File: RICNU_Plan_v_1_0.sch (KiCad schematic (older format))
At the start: 0 parts

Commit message: Re-routed CAN, RS-485, and debug connectors (wrong polarity in all)
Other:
- note added: "*"
- note added: "A and B for SN65HVD75 are \nopposite of RS-485 standard"
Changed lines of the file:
@@
 F0 "RS485 Transceiver" 60
 F1 "RICNU_Plan_v_1_0_RS485.sch" 60
-F2 "RS485.A" B L 3800 4500 60
-F3 "RS485.B" B L 3800 4600 60
+F2 "RS485.A" B L 3800 4600 60
+F3 "RS485.B" B L 3800 4500 60
 F4 "RS485.#RE" I R 5500 4700 60
 F5 "RS485.DE" I R 5500 4600 60
@@
 F4 "SWD.RESET" O R 3100 3300 60
 $EndSheet
+Text Notes 2800 6700 0    60   ~ 0
+A and B for SN65HVD75 are \nopposite of RS-485 standard
+Text Notes 4300 4500 0    60   ~ 0
+*
+Text Notes 2700 6600 0    60   ~ 0
+*
 $EndSCHEMATC

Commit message: Added connections to monitor power, changed CANSTB MCU pin, moved LED pins around
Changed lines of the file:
@@
 $EndDescr
 $Sheet
-S 3798 5702 1702 298
+S 3798 5902 1702 298
 U 59D46777
 F0 "Power Conditioning" 60
@@
 $EndSheet
 $Sheet
-S 6200 5150 1700 850
+S 6200 5350 1700 850
 U 59E3791C
 F0 "Bus Driver" 60
 F1 "RICNU_Plan_v_1_0_UARTDriver.sch" 60
-F2 "UMUX.BT.TX" I R 7900 5800 60
-F3 "UMUX.BT.RX" O R 7900 5900 60
-F4 "UMUX.U2U.RX" O L 6200 5250 60
-F5 "UMUX.U2U.TX" I L 6200 5350 60
-F6 "UMUX.MCU.RX" O R 7900 5250 60
-F7 "UMUX.MCU.TX" I R 7900 5350 60
-F8 "UMUX.BT.BOOT" O R 7900 5700 60
-$EndSheet
-$Sheet
-S 3800 5150 1700 300
+F2 "UMUX.BT.TX" I R 7900 6000 60
+F3 "UMUX.BT.RX" O R 7900 6100 60
+F4 "UMUX.U2U.RX" O L 6200 5450 60
+F5 "UMUX.U2U.TX" I L 6200 5550 60
+F6 "UMUX.MCU.RX" O R 7900 5450 60
+F7 "UMUX.MCU.TX" I R 7900 5550 60
+F8 "UMUX.BT.BOOT" O R 7900 5900 60
+$EndSheet
+$Sheet
+S 3800 5150 1700 500
 U 59D3E543
 F0 "USB to UART" 60
 F1 "RICNU_Plan_v_1_0_USB2UART.sch" 60
-F2 "U2U.TX" O R 5500 5350 60
-F3 "U2U.RX" I R 5500 5250 60
+F2 "U2U.TX" O R 5500 5550 60
+F3 "U2U.RX" I R 5500 5450 60
 F4 "U2U.USB.DP" B L 3800 5250 60
 F5 "U2U.USB.DM" B L 3800 5350 60
+F6 "U2U.PWREN" O R 5500 5250 60
+F7 "U2U.USBON" O R 5500 5350 60
 $EndSheet
 $Sheet
@@
 Series protection resistor included in "Breakout"
 $Sheet
-S 8600 5600 1700 400
+S 8600 5800 1700 400
 U 59D3E54A
 F0 "Bluetooth" 60
 F1 "RICNU_Plan_v_1_0_Bluetooth.sch" 60
-F2 "BT.BOOT0" I L 8600 5700 60
-F3 "BT.RX" I L 8600 5900 60
-F4 "BT.TX" O L 8600 5800 60
+F2 "BT.BOOT0" I L 8600 5900 60
+F3 "BT.RX" I L 8600 6100 60
+F4 "BT.TX" O L 8600 6000 60
 $EndSheet
 Text Notes 6750 9100 0    60   ~ 0
@@
 Open copper ring around the periphery of the board\nstitched throughout with vias & connected to USB shield \nand SD card shield. - ESD protection and edge EMC.\nAn external ESD strike will prefer the ring/shield casing for SD/USB instead \nof the components, and will be either earthed if connected to PC+wall\nor discharged into board ground via multiple small caps (see SD and USB).\nIf on the knee, discharged into the screw(s?) and into the metal leg
 $Sheet
-S 6200 1400 1700 3500
+S 6200 1400 1700 3700
 U 59D3E349
 F0 "MCU" 60
@@
 F42 "MCU.PC7" B R 7900 1900 60
 F43 "MCU.PA0" B R 7900 1500 60
+F44 "MCU.PWREN" I L 6200 4900 60
+F45 "MCU.USBON" I L 6200 5000 60
 $EndSheet
 Text Notes 10400 9200 0    60   ~ 0
@@
 	5500 4800 6200 4800
 Wire Wire Line
-	5500 5250 6200 5250
-Wire Wire Line
-	5500 5350 6200 5350
-Wire Wire Line
-	7900 5250 8600 5250
-Wire Wire Line
-	8600 5250 8600 4800
+	5500 5450 6200 5450
+Wire Wire Line
+	5500 5550 6200 5550
+Wire Wire Line
+	7900 5450 8600 5450
+Wire Wire Line
+	8600 5450 8600 4800
 Wire Wire Line
 	8600 4800 7900 4800
@@
 	7900 4700 8700 4700
 Wire Wire Line
-	8700 4700 8700 5350
-Wire Wire Line
-	8700 5350 7900 5350
-Wire Wire Line
-	8600 5700 7900 5700
-Wire Wire Line
-	8600 5800 7900 5800
+	8700 4700 8700 5550
+Wire Wire Line
+	8700 5550 7900 5550
 Wire Wire Line
 	8600 5900 7900 5900
+Wire Wire Line
+	8600 6000 7900 6000
+Wire Wire Line
+	8600 6100 7900 6100
 $Sheet
 S 8600 1400 1700 1700
@@
 Text Label 5550 4800 0    60   ~ 0
 RS485_RX
-Text Label 5550 5250 0    60   ~ 0
+Text Label 5550 5450 0    60   ~ 0
 FTDI_UART_RX
-Text Label 5550 5350 0    60   ~ 0
+Text Label 5550 5550 0    60   ~ 0
 FTDI_UART_TX
 Text Label 3150 5250 0    60   ~ 0
@@
 Text Label 3150 4500 0    60   ~ 0
 RS485_D+
-Text Label 7950 5350 0    60   ~ 0
+Text Label 7950 5550 0    60   ~ 0
 MCU_UART_TX
-Text Label 7950 5250 0    60   ~ 0
+Text Label 7950 5450 0    60   ~ 0
 MCU_UART_RX
-Text Label 7950 5700 0    60   ~ 0
+Text Label 7950 5800 0    60   ~ 0
 BT_BOOT0
-Text Label 7950 5800 0    60   ~ 0
+Text Label 7950 5900 0    60   ~ 0
 BT_UART_TX
-Text Label 7950 5900 0    60   ~ 0
+Text Label 7950 6000 0    60   ~ 0
 BT_UART_RX
 Wire Wire Line
@@
 DIO16
 $Sheet
-S 1400 5700 1700 300
+S 1400 5900 1700 300
 U 59FC1385
 F0 "5V Power Input Connector" 60
@@
 Text Notes 2700 6600 0    60   ~ 0
 *
+Wire Wire Line
+	6200 4900 6000 4900
+Wire Wire Line
+	6000 4900 6000 5250
+Wire Wire Line
+	6000 5250 5500 5250
+Wire Wire Line
+	5500 5350 6100 5350
+Wire Wire Line
+	6100 5350 6100 5000
+Wire Wire Line
+	6100 5000 6200 5000
+Text Label 5550 5350 0    60   ~ 0
+FTDI_USBON
+Text Label 5550 5250 0    60   ~ 0
+FTDI_PWREN
 $EndSCHEMATC

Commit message: Design freeze - ordered the board
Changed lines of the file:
@@
 Text Label 7950 5450 0    60   ~ 0
 MCU_UART_RX
-Text Label 7950 5800 0    60   ~ 0
+Text Label 8000 5900 0    60   ~ 0
 BT_BOOT0
-Text Label 7950 5900 0    60   ~ 0
+Text Label 8000 6000 0    60   ~ 0
 BT_UART_TX
-Text Label 7950 6000 0    60   ~ 0
+Text Label 8000 6100 0    60   ~ 0
 BT_UART_RX
 Wire Wire Line

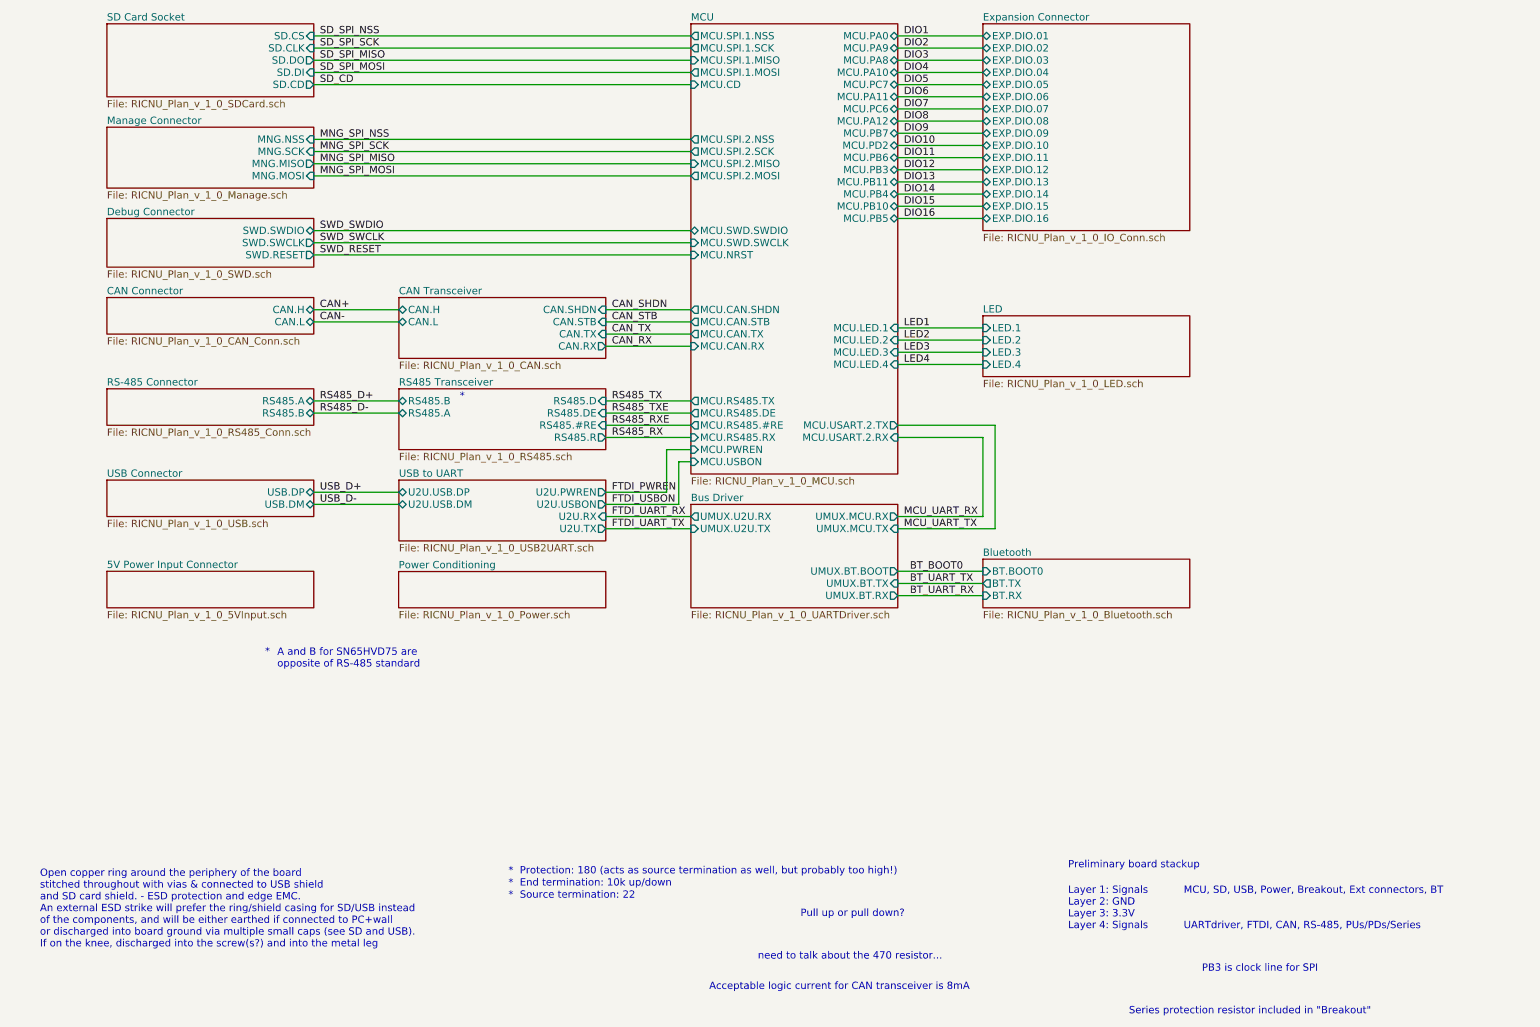
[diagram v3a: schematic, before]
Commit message: Deleting PDFs
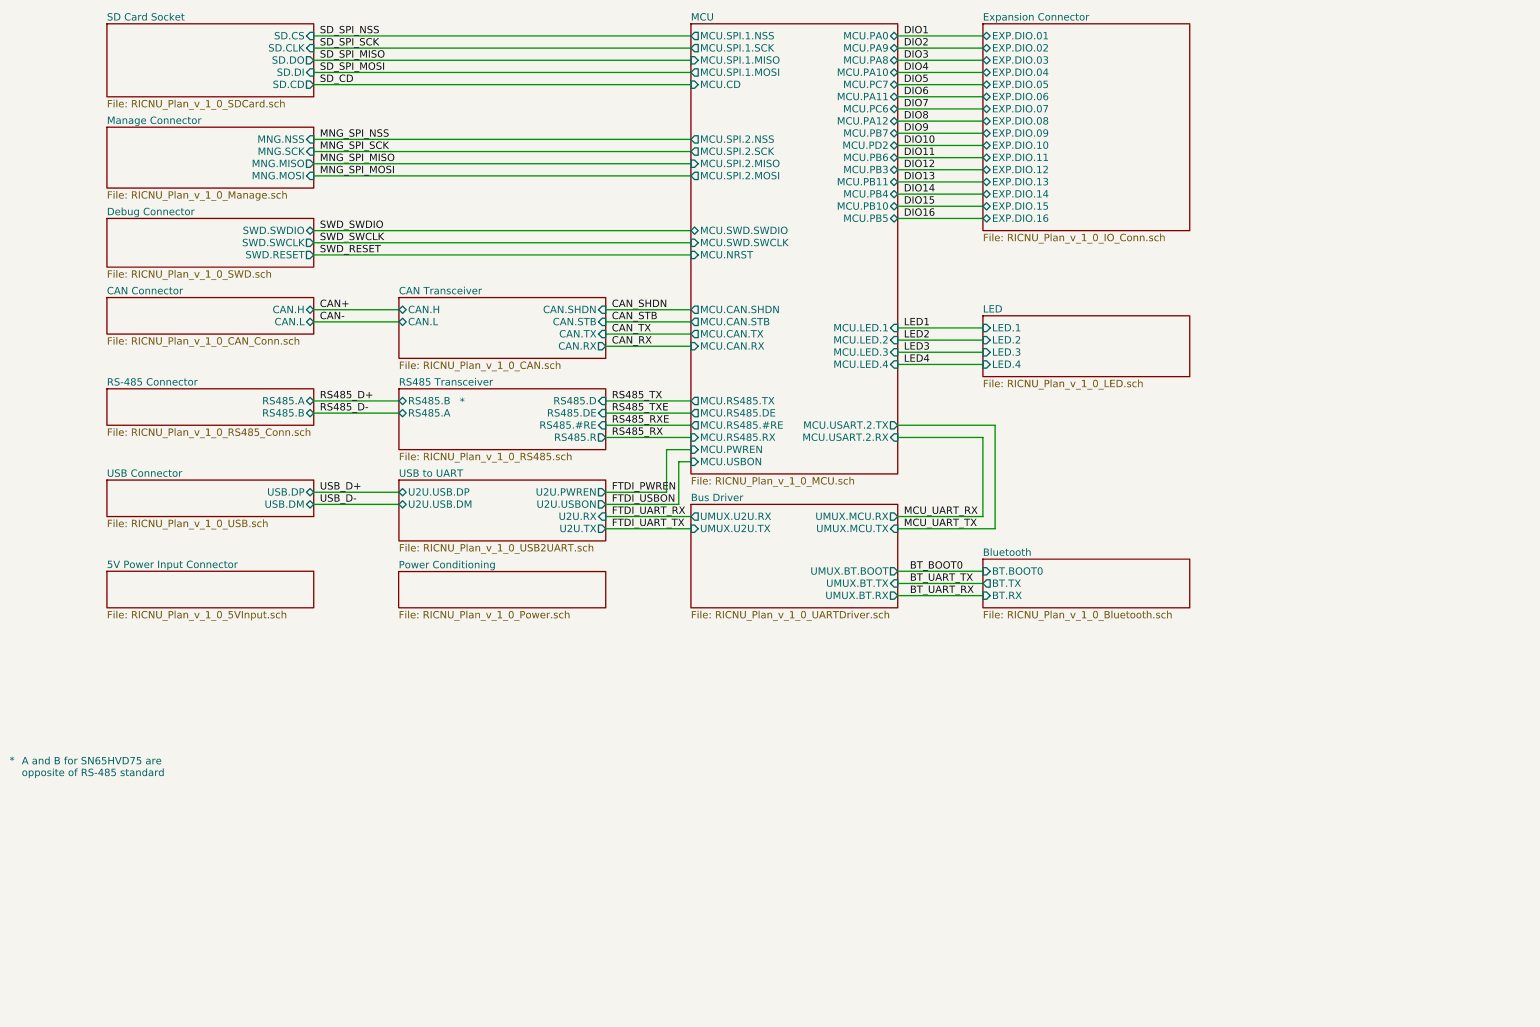
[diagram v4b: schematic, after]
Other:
- note removed: "* End termination: 10k up/down"
- note removed: "* Protection: 180 (acts as source termination as well, but probably too high!)"
- note removed: "* Source termination: 22"
- note removed: "Acceptable logic current for CAN transceiver is 8mA"
- note removed: "Layer 1: Signals\nLayer 2: GND\nLayer 3: 3.3V\nLayer 4: Signals"
- note removed: "MCU, SD, USB, Power, Breakout, Ext connectors, BT\n\n\nUARTdriver, FTDI, CAN, RS-485, PUs/PDs/Series"
- note removed: "Open copper ring around the periphery of the board\nstitched throughout with vias & connected to USB shield \nand SD card shield. - ESD protection and edge EMC.\nAn external ESD strike will prefer the ring/shield casing for SD/USB instead \nof the components, and will be either earthed if connected to PC+wall\nor discharged into board ground via multiple small caps (see SD and USB).\nIf on the kn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"
- note removed: "PB3 is clock line for SPI"
- note removed: "Preliminary board stackup"
- note removed: "Pull up or pull down?"
- note removed: "Series protection resistor included in "Breakout""
- note removed: "need to talk about the 470 resistor..."
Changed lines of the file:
@@
 F7 "RS485.R" O R 5500 4800 60
 $EndSheet
-Text Notes 7100 8750 0    60   ~ 0
-Pull up or pull down?
-Text Notes 4700 8400 0    60   ~ 0
-*  Protection: 180 (acts as source termination as well, but probably too high!)
-Text Notes 4700 8500 0    60   ~ 0
-*  End termination: 10k up/down
-Text Notes 4700 8600 0    60   ~ 0
-*  Source termination: 22
-Text Notes 6350 9350 0    60   ~ 0
-Acceptable logic current for CAN transceiver is 8mA
-Text Notes 9800 9550 0    60   ~ 0
-Series protection resistor included in "Breakout"
 $Sheet
 S 8600 5800 1700 400
@@
 F4 "BT.TX" O L 8600 6000 60
 $EndSheet
-Text Notes 6750 9100 0    60   ~ 0
-need to talk about the 470 resistor...
-Text Notes 850  9000 0    60   ~ 0
-Open copper ring around the periphery of the board\nstitched throughout with vias & connected to USB shield \nand SD card shield. - ESD protection and edge EMC.\nAn external ESD strike will prefer the ring/shield casing for SD/USB instead \nof the components, and will be either earthed if connected to PC+wall\nor discharged into board ground via multiple small caps (see SD and USB).\nIf on the knee, discharged into the screw(s?) and into the metal leg
 $Sheet
 S 6200 1400 1700 3700
@@
 F45 "MCU.USBON" I L 6200 5000 60
 $EndSheet
-Text Notes 10400 9200 0    60   ~ 0
-PB3 is clock line for SPI
-Text Notes 9300 8850 0    60   ~ 0
-Layer 1: Signals\nLayer 2: GND\nLayer 3: 3.3V\nLayer 4: Signals
-Text Notes 10250 8850 0    60   ~ 0
-MCU, SD, USB, Power, Breakout, Ext connectors, BT\n\n\nUARTdriver, FTDI, CAN, RS-485, PUs/PDs/Series
-Text Notes 9300 8350 0    60   ~ 0
-Preliminary board stackup
 $Sheet
 S 1400 5150 1700 300
@@
 F4 "SWD.RESET" O R 3100 3300 60
 $EndSheet
-Text Notes 2800 6700 0    60   ~ 0
+Text Notes 700  7600 0    60   ~ 0
 A and B for SN65HVD75 are \nopposite of RS-485 standard
-Text Notes 4300 4500 0    60   ~ 0
+Text Notes 4300 4550 0    60   ~ 0
 *
-Text Notes 2700 6600 0    60   ~ 0
+Text Notes 600  7500 0    60   ~ 0
 *
 Wire Wire Line
